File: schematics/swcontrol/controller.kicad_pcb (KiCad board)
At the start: 2 copper layers, 7 parts, among them P1 BK24x1, P2 BSL, P3 PWRBRD, U1 MSP430F1222IDW

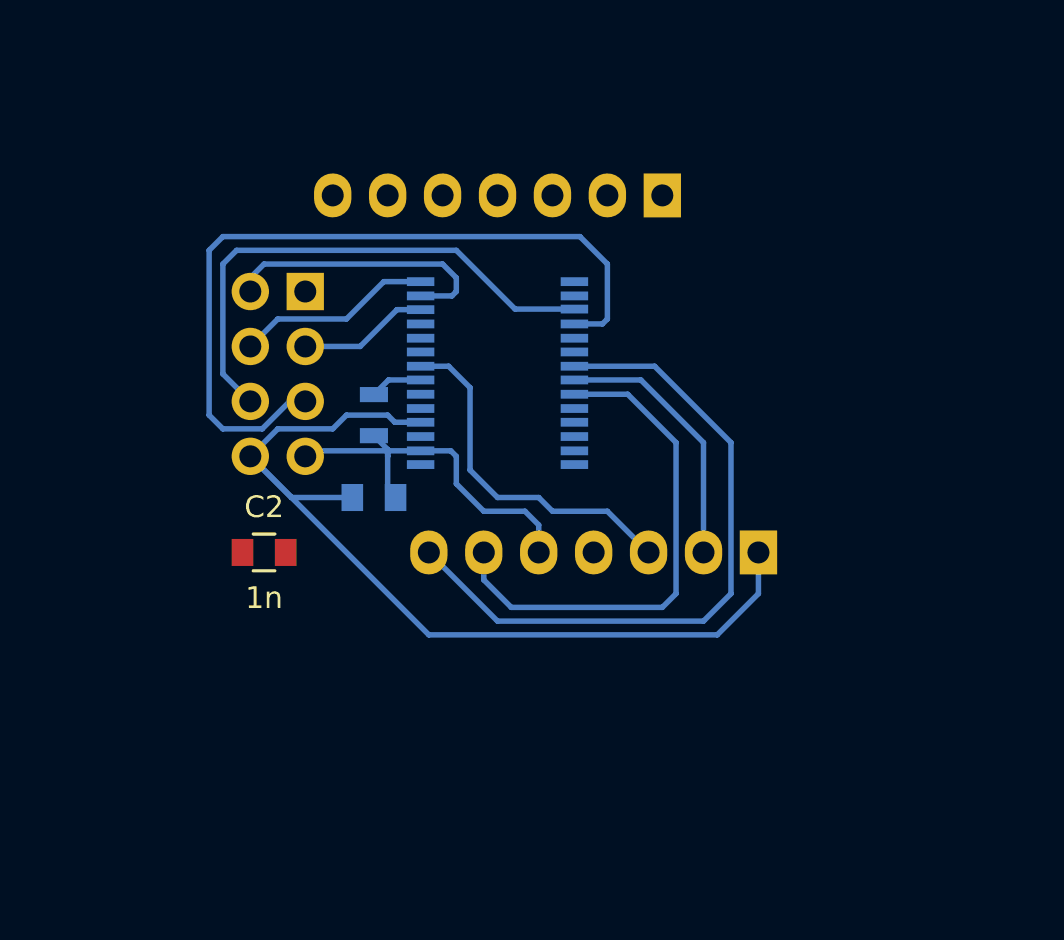
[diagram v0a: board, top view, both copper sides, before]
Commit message: Changing uC
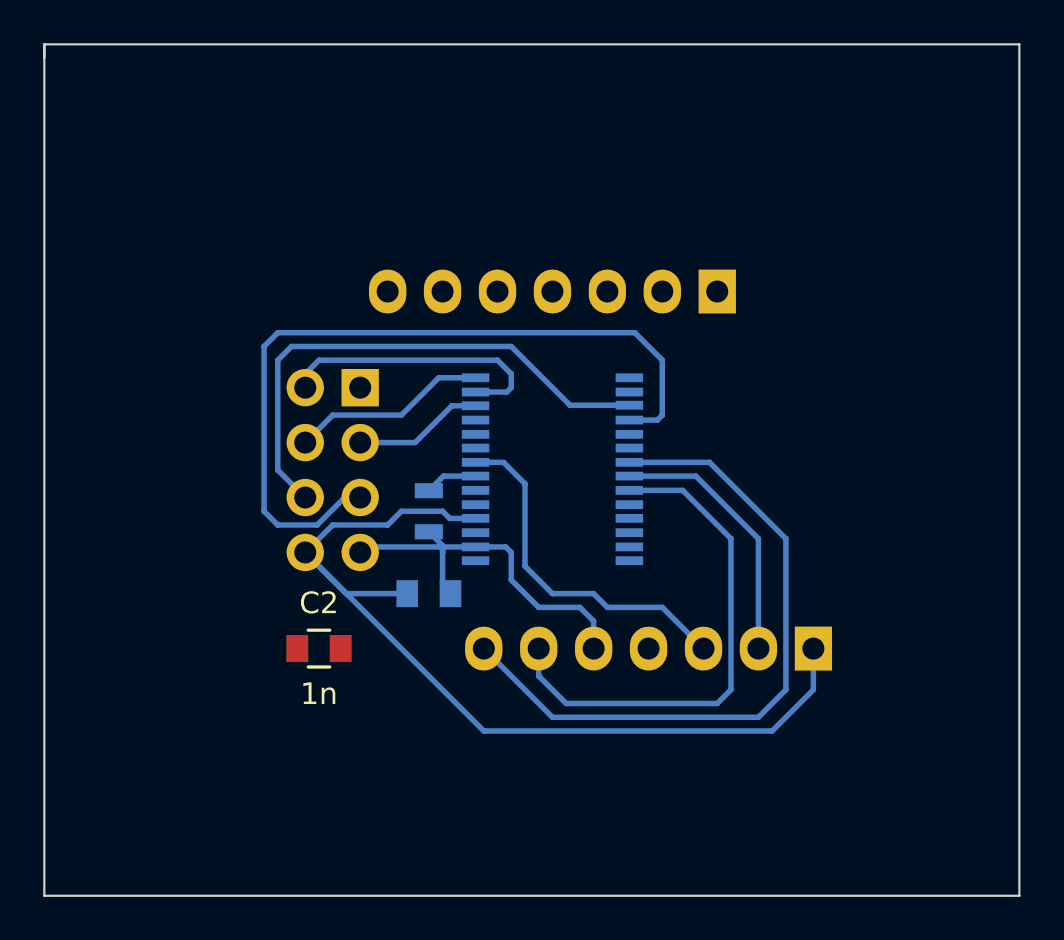
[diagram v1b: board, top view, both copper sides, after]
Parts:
- moved P1 5.12 mm to (137.2, 109.9)
- moved R1 5.12 mm to (141.6, 111.8)
- moved U1 5.12 mm to (147.3, 109.9)
- moved C1 5.12 mm to (141.6, 115.6)
- moved C2 5.12 mm to (136.5, 118.1)
- moved P2 5.12 mm to (147.3, 101.6)
- moved P3 5.12 mm to (151.8, 118.1)
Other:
- board outline added: 45.1 x 39.4 mm
